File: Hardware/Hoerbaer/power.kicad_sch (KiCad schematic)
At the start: 49 parts, among them J12 Battery 1S Li-Ion, Q1 DMG3415UQ-7, U12 MAX17048G, U13 TPS61288, U8 MCP73831T-2ACI/OT (4.2V), U9 TPS63001

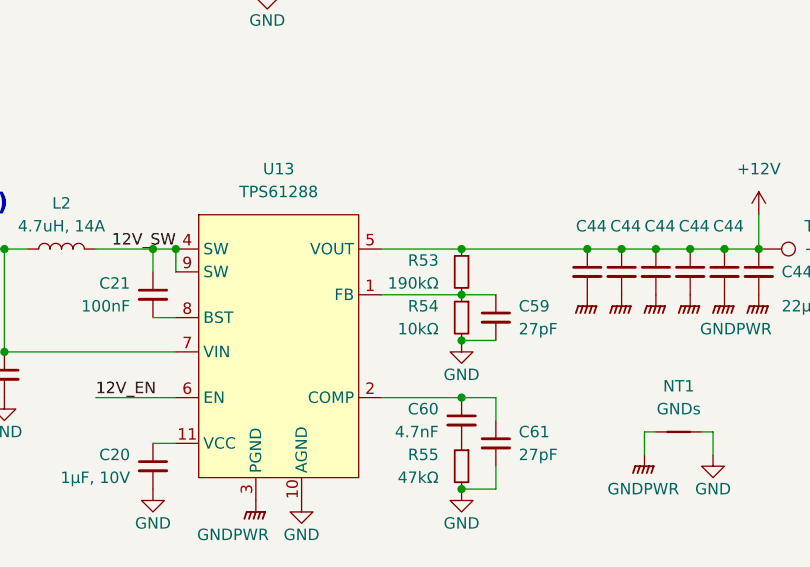
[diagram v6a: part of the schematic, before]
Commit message: Resistor Order Numbers
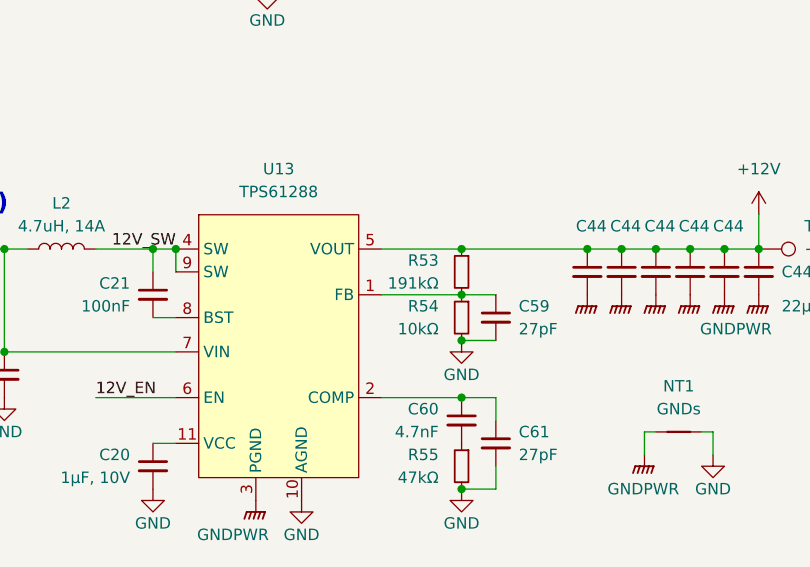
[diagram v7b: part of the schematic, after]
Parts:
- R11, R54: LCSC (none) -> C25744; MPN (none) -> 0402WGF1002TCE
- R11: LCSC (none) -> C25741; MPN (none) -> 0402WGF1003TCE
- R11: LCSC (none) -> C25076; MPN (none) -> 0402WGF1000TCE
- R53: value 190kΩ -> 191kΩ; LCSC (none) -> C270632; MPN (none) -> 0402WGF1913TCE
- R55: LCSC (none) -> C25792; MPN (none) -> 0402WGF4702TCE
- R62: LCSC (none) -> C4109; MPN (none) -> 0402WGF2001TCE
- TP10, TP4, TP5, TP6, TP7, TP8, TP9: now left out of the parts list
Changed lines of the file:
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@@
+      (effects (font (size 1.27 1.27)) hide)
+    )
+    (property "LCSC" "C25744" (at 38.1 170.18 0)
+      (effects (font (size 1.27 1.27)) hide)
+    )
+    (property "MPN" "0402WGF1002TCE" (at 38.1 170.18 0)
       (effects (font (size 1.27 1.27)) hide)
     )
@@
   )
   (symbol (lib_id "Connector:TestPoint") (at 181.61 43.18 270) (unit 1)
-    (in_bom yes) (on_board yes) (dnp no)
+    (in_bom no) (on_board yes) (dnp no)
     (property "Reference" "TP4" (at 186.69 40.64 90)
       (effects (font (size 1.27 1.27)) (justify left))
@@
       (effects (font (size 1.27 1.27)) (justify left))
     )
-    (property "Value" "190kΩ" (at 153.67 102.87 0)
+    (property "Value" "191kΩ" (at 153.67 102.87 0)
       (effects (font (size 1.27 1.27)) (justify left))
     )
@@
     )
     (property "Datasheet" "~" (at 156.21 101.6 0)
+      (effects (font (size 1.27 1.27)) hide)
+    )
+    (property "LCSC" "C270632" (at 156.21 101.6 0)
+      (effects (font (size 1.27 1.27)) hide)
+    )
+    (property "MPN" "0402WGF1913TCE" (at 156.21 101.6 0)
       (effects (font (size 1.27 1.27)) hide)
     )
@@
       (effects (font (size 1.27 1.27)) hide)
     )
+    (property "LCSC" "C25741" (at 39.37 50.8 0)
+      (effects (font (size 1.27 1.27)) hide)
+    )
+    (property "MPN" "0402WGF1003TCE" (at 39.37 50.8 0)
+      (effects (font (size 1.27 1.27)) hide)
+    )
     (pin "1")
     (pin "2")
@@
     )
     (property "Datasheet" "~" (at 107.95 45.72 0)
+      (effects (font (size 1.27 1.27)) hide)
+    )
+    (property "LCSC" "C25076" (at 107.95 45.72 0)
+      (effects (font (size 1.27 1.27)) hide)
+    )
+    (property "MPN" "0402WGF1000TCE" (at 107.95 45.72 0)
       (effects (font (size 1.27 1.27)) hide)
     )
@@
   )
   (symbol (lib_id "Connector:TestPoint") (at 48.26 172.72 180) (unit 1)
-    (in_bom yes) (on_board yes) (dnp no)
+    (in_bom no) (on_board yes) (dnp no)
     (property "Reference" "TP8" (at 53.34 173.99 0)
       (effects (font (size 1.27 1.27)) (justify left))
@@
       (effects (font (size 1.27 1.27)) hide)
     )
+    (property "LCSC" "C25792" (at 156.21 123.19 0)
+      (effects (font (size 1.27 1.27)) hide)
+    )
+    (property "MPN" "0402WGF4702TCE" (at 156.21 123.19 0)
+      (effects (font (size 1.27 1.27)) hide)
+    )
     (pin "1")
     (pin "2")
@@
       (effects (font (size 1.27 1.27)) hide)
     )
+    (property "LCSC" "C25744" (at 156.21 106.68 0)
+      (effects (font (size 1.27 1.27)) hide)
+    )
+    (property "MPN" "0402WGF1002TCE" (at 156.21 106.68 0)
+      (effects (font (size 1.27 1.27)) hide)
+    )
     (pin "1")
     (pin "2")
@@
     )
     (property "Datasheet" "~" (at 257.81 55.88 0)
+      (effects (font (size 1.27 1.27)) hide)
+    )
+    (property "LCSC" "C4109" (at 257.81 55.88 0)
+      (effects (font (size 1.27 1.27)) hide)
+    )
+    (property "MPN" "0402WGF2001TCE" (at 257.81 55.88 0)
       (effects (font (size 1.27 1.27)) hide)
     )
@@
   )
   (symbol (lib_id "Connector:TestPoint") (at 245.11 139.7 0) (unit 1)
-    (in_bom yes) (on_board yes) (dnp no)
+    (in_bom no) (on_board yes) (dnp no)
     (property "Reference" "TP5" (at 242.57 134.62 90)
       (effects (font (size 1.27 1.27)) (justify left))
@@
   )
   (symbol (lib_id "Connector:TestPoint") (at 48.26 135.89 180) (unit 1)
-    (in_bom yes) (on_board yes) (dnp no)
+    (in_bom no) (on_board yes) (dnp no)
     (property "Reference" "TP6" (at 53.34 137.16 0)
       (effects (font (size 1.27 1.27)) (justify left))
@@
   )
   (symbol (lib_id "Connector:TestPoint") (at 48.26 149.86 180) (unit 1)
-    (in_bom yes) (on_board yes) (dnp no)
+    (in_bom no) (on_board yes) (dnp no)
     (property "Reference" "TP7" (at 53.34 151.13 0)
       (effects (font (size 1.27 1.27)) (justify left))
@@
     )
     (property "Datasheet" "~" (at 38.1 182.88 0)
+      (effects (font (size 1.27 1.27)) hide)
+    )
+    (property "LCSC" "C25744" (at 38.1 182.88 0)
+      (effects (font (size 1.27 1.27)) hide)
+    )
+    (property "MPN" "0402WGF1002TCE" (at 38.1 182.88 0)
       (effects (font (size 1.27 1.27)) hide)
     )
@@
   )
   (symbol (lib_id "Connector:TestPoint") (at 189.23 99.06 270) (unit 1)
-    (in_bom yes) (on_board yes) (dnp no)
+    (in_bom no) (on_board yes) (dnp no)
     (property "Reference" "TP10" (at 194.31 96.52 90)
       (effects (font (size 1.27 1.27)) (justify left))
@@
     )
     (property "Datasheet" "~" (at 38.1 152.4 0)
+      (effects (font (size 1.27 1.27)) hide)
+    )
+    (property "LCSC" "C25744" (at 38.1 152.4 0)
+      (effects (font (size 1.27 1.27)) hide)
+    )
+    (property "MPN" "0402WGF1002TCE" (at 38.1 152.4 0)
       (effects (font (size 1.27 1.27)) hide)
     )
@@
   )
   (symbol (lib_id "Connector:TestPoint") (at 48.26 185.42 180) (unit 1)
-    (in_bom yes) (on_board yes) (dnp no)
+    (in_bom no) (on_board yes) (dnp no)
     (property "Reference" "TP9" (at 53.34 186.69 0)
       (effects (font (size 1.27 1.27)) (justify left))
@@
       (effects (font (size 1.27 1.27)) hide)
     )
+    (property "LCSC" "C25744" (at 38.1 138.43 0)
+      (effects (font (size 1.27 1.27)) hide)
+    )
+    (property "MPN" "0402WGF1002TCE" (at 38.1 138.43 0)
+      (effects (font (size 1.27 1.27)) hide)
+    )

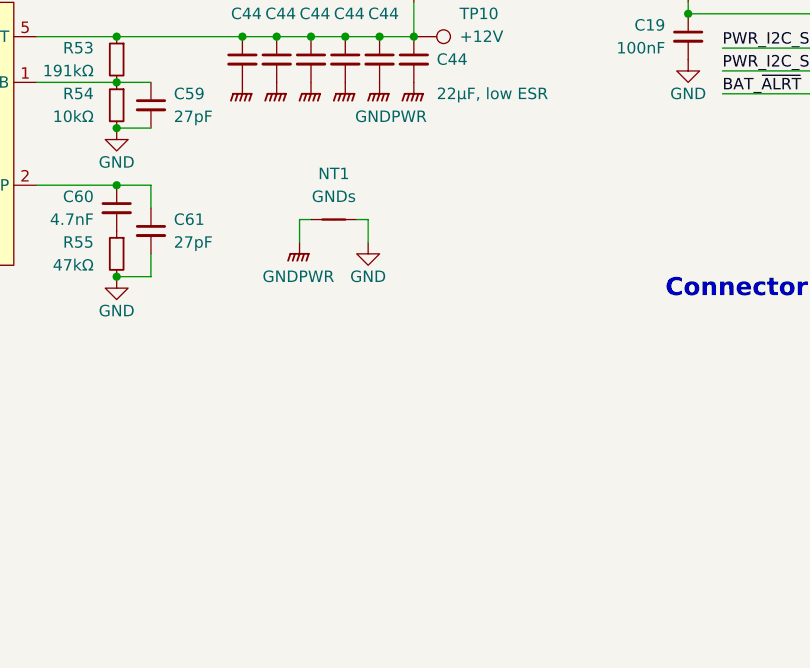
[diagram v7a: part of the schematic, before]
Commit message: Fixed net tie ground plane issue.
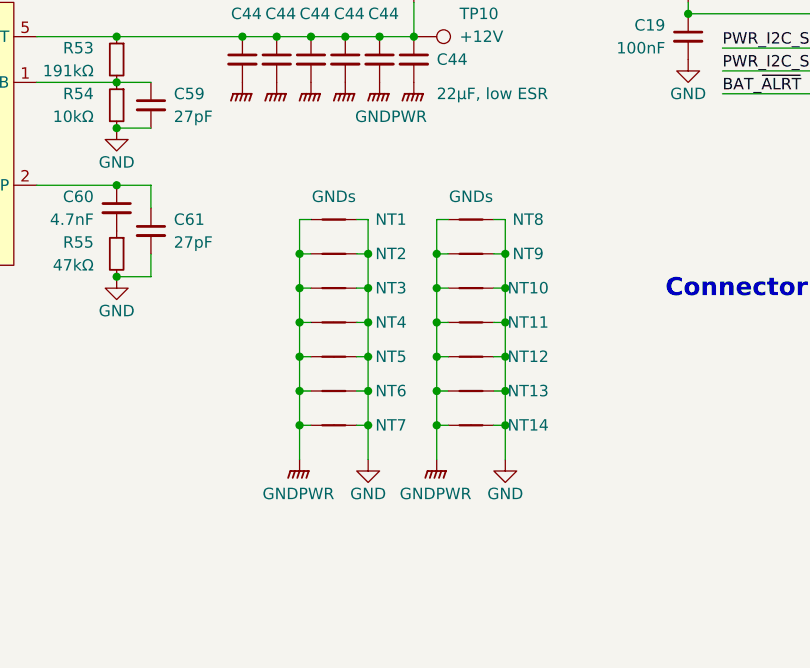
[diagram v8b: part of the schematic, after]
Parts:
- added NT10, NT11, NT12, NT13, NT14, NT2, NT3, NT4, NT5, NT6, NT7, NT8, NT9: GNDs, Baer_Footprints:NetTie-2_Via, symbol Device:NetTie_2
- NT1: footprint NetTie:NetTie-2_THT_Pad0.3mm -> Baer_Footprints:NetTie-2_Via
- U12, U8: JLCPCB Rotation Offset (none) -> 90
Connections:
- net GND: now also NT10.2, NT11.2, NT12.2, NT13.2, NT14.2, NT2.2, NT3.2, NT4.2, NT5.2, NT6.2, NT7.2, NT8.2, NT9.2
- net GNDPWR: now also NT10.1, NT11.1, NT12.1, NT13.1, NT14.1, NT2.1, NT3.1, NT4.1, NT5.1, NT6.1, NT7.1, NT8.1, NT9.1
